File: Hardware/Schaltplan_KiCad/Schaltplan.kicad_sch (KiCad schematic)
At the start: 59 parts, among them J1 3-106505-2, J2 USB_B_Micro, J3 Conn_01x04_Pin, J4 Conn_01x02_Pin, SW1 SW_Omron_B3FS, SW2 SW_Omron_B3FS, SW3 SW_Omron_B3FS, U1 MCP2562-E-SN, U2 FT231XS, U3 ESP32-DEVKITC-32U, U4 AZ1117-5.0, U5 PCA9306DCTR

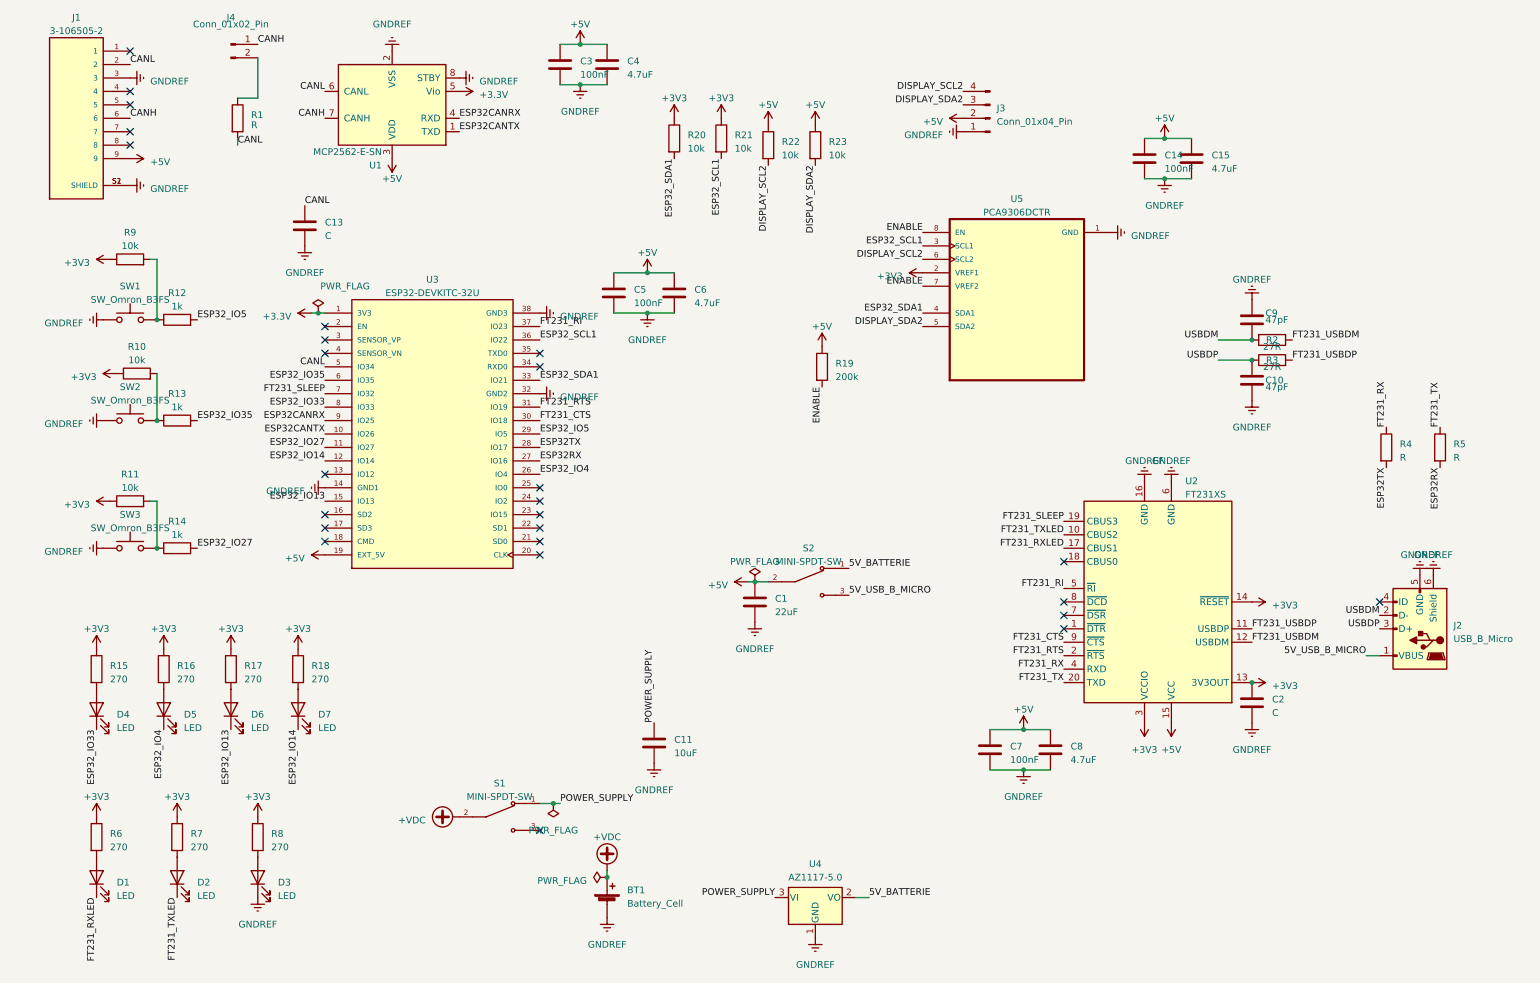
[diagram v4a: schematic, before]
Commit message: changed switch and ldo
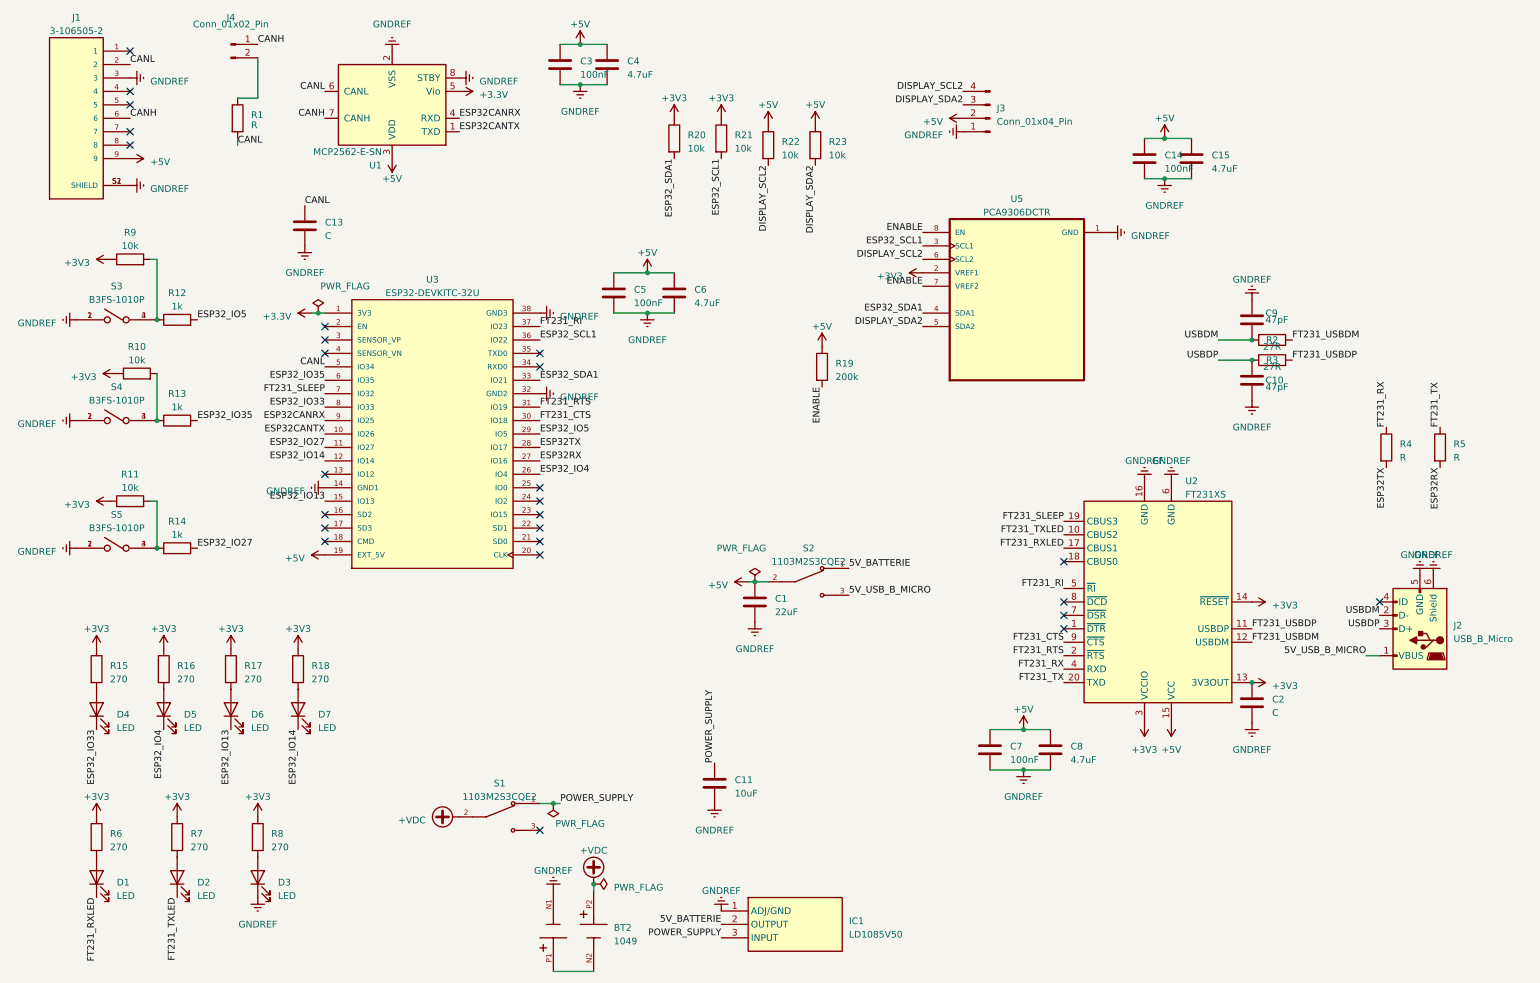
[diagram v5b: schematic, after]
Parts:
- removed BT1: Battery_Cell, symbol Device:Battery_Cell
- removed SW1, SW2, SW3: SW_Omron_B3FS, Button:SW_B3FS-1010P, symbol Switch:SW_Omron_B3FS
- removed U4: AZ1117-5.0, LDO:SOT150P410X160-3N, symbol Regulator_Linear:AZ1117-5.0
- added BT2: 1049, battery_holder:BAT_1049, symbol 1049:1049
- added IC1: LD1085V50, LDO:TO255P460X1020X2008-3P, symbol LD1085V50:LD1085V50
- added S3, S4, S5: B3FS-1010P, SW_B3FS-1010P, symbol B3FS-1010P:B3FS-1010P
- S1, S2: value MINI-SPDT-SW -> 1103M2S3CQE2; footprint switches:SW_MINI-SPDT-SW -> switches:SW_1103M2S3CQE2
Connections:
- net +VDC: now also BT2.P2
- net 5V_BATTERIE: now also IC1.2 (OUTPUT)
- net GNDREF: now also BT2.N1, IC1.1 (ADJ/GND), S3.1, S3.2, S4.1, S4.2, S5.1, S5.2
- net POWER_SUPPLY: now also IC1.3 (INPUT)
- net at R11.2, R14.1: now also S5.3, S5.4
- net at R10.2, R13.1: now also S4.3, S4.4
- net at R12.1, R9.2: now also S3.3, S3.4
- new net: BT2.N2, BT2.P1
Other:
- moved on the sheet: C11

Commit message: placed components on pcb
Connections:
- net +3.3V is gone; now on net +3V3: U1.5 (Vio), U3.1 (3V3)
- net +3V3: no longer C2.1, R6.1, R7.1, R8.1, U2.13 (3V3OUT), U2.14 (~{RESET}), U2.3 (VCCIO)
- net +5V: now also R8.1
- new net FT231_3V3_OUT: C2.1, R6.1, R7.1, U2.13 (3V3OUT), U2.14 (~{RESET}), U2.3 (VCCIO)

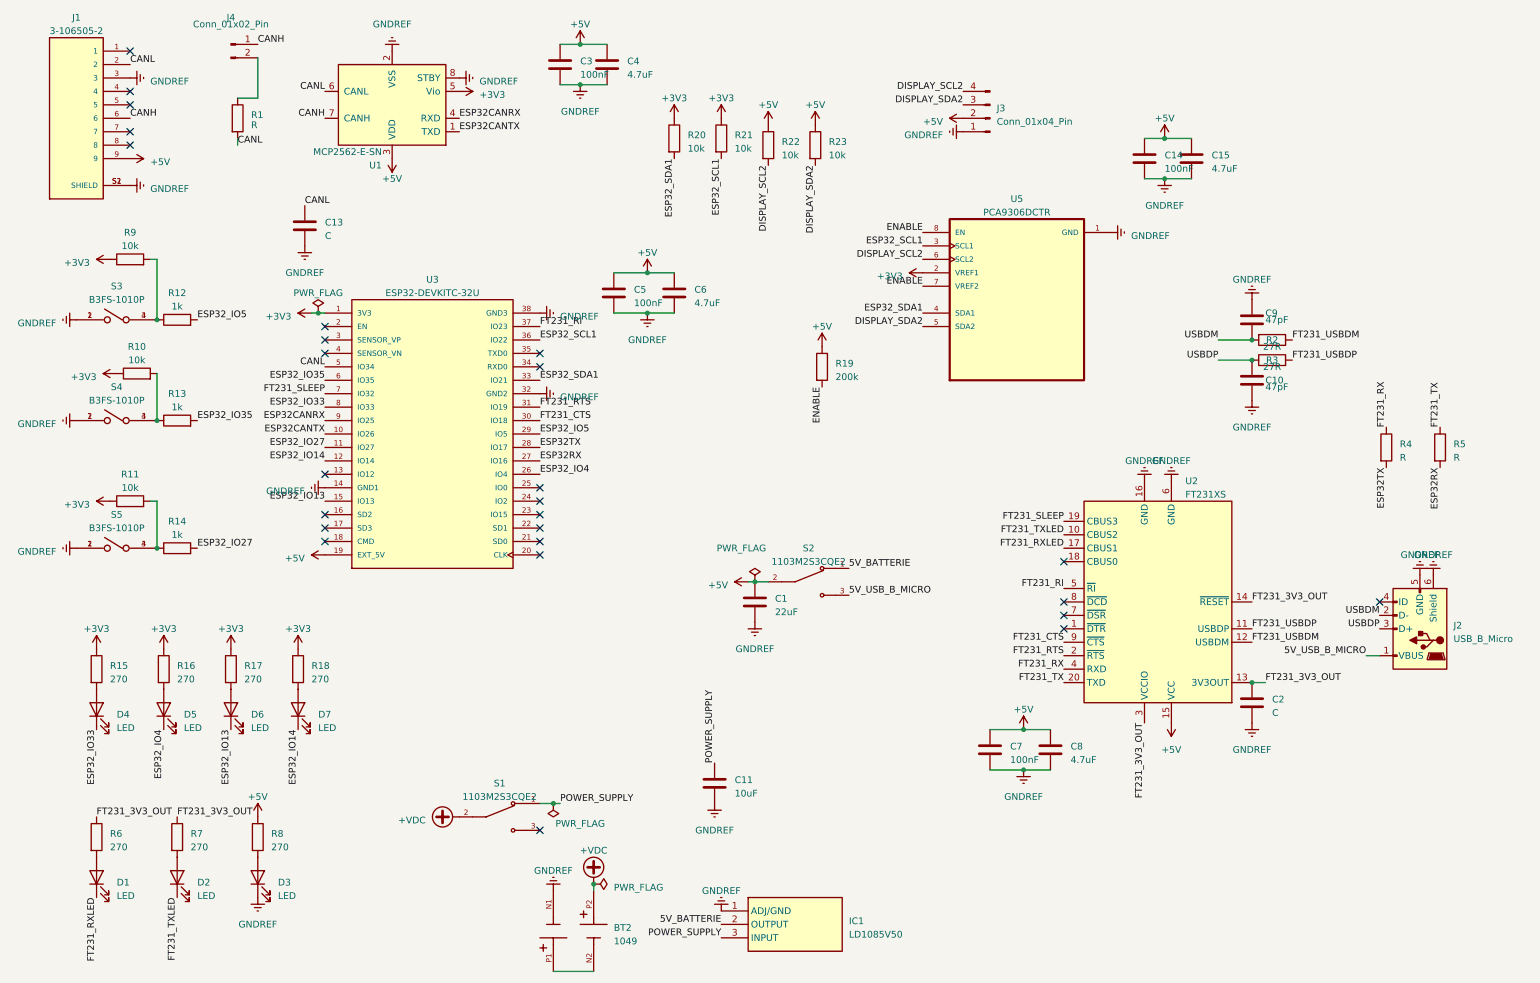
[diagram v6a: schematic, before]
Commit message: remove battery and redesign
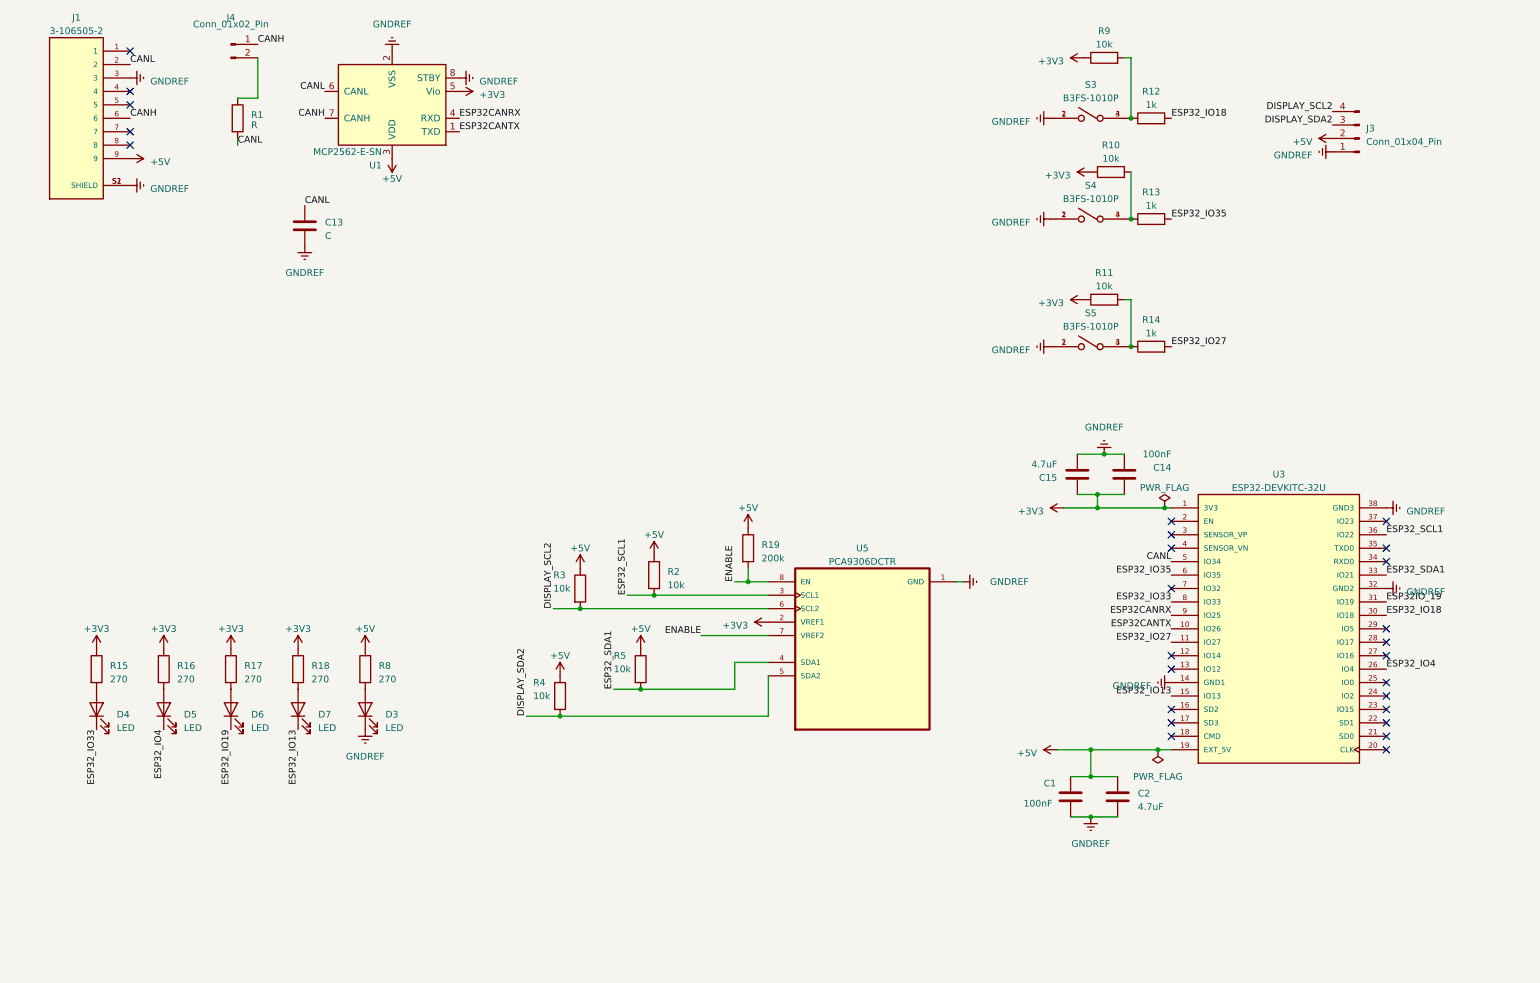
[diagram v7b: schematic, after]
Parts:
- removed BT2: 1049, battery_holder:BAT_1049, symbol 1049:1049
- removed C10, C9: 47pF, Capacitor_SMD:C_1812_4532Metric_Pad1.57x3.40mm_HandSolder, symbol Device:C
- removed C11: 10uF, Capacitor_SMD:C_1812_4532Metric_Pad1.57x3.40mm_HandSolder, symbol Device:C
- removed C3, C5, C7: 100nF, Capacitor_SMD:C_1812_4532Metric_Pad1.57x3.40mm_HandSolder, symbol Device:C
- removed C4, C6, C8: 4.7uF, Capacitor_SMD:C_1812_4532Metric_Pad1.57x3.40mm_HandSolder, symbol Device:C
- removed D1, D2: LED, LED:LED_OF-SMD3528WC, symbol Device:LED
- removed IC1: LD1085V50, LDO:TO255P460X1020X2008-3P, symbol LD1085V50:LD1085V50
- removed J2: USB_B_Micro, Connector_USB:USB_Micro-B_Amphenol_10103594-0001LF_Horizontal, symbol Connector:USB_B_Micro
- removed R20, R21, R22, R23: 10k, Resistor_SMD:R_2010_5025Metric_Pad1.40x2.65mm_HandSolder, symbol Device:R
- removed R6, R7: 270, Resistor_SMD:R_2010_5025Metric_Pad1.40x2.65mm_HandSolder, symbol Device:R
- removed S1, S2: 1103M2S3CQE2, switches:SW_1103M2S3CQE2, symbol MINI-SPDT-SW:MINI-SPDT-SW
- removed U2: FT231XS, USB2UART:SOP63P600X175-20N, symbol Interface_USB:FT231XS
- C1: value 22uF -> 100nF
- C2: value C -> 4.7uF
- R2, R3: value 27R -> 10k
- R4, R5: value R -> 10k
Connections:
- net FT231_3V3_OUT is gone; now on net +5V: C2.1
- net FT231_RX is gone; now on net +5V: R4.1
- net FT231_TX is gone; now on net +5V: R5.1
- net FT231_USBDM is gone; now on net +5V: R2.1
- net FT231_USBDP is gone; now on net DISPLAY_SCL2: R3.2
- net USBDM is gone; now on net ESP32_SCL1: R2.2
- net USBDP is gone; now on net +5V: R3.1
- net +3V3: now also C14.1, C15.1
- net +5V: no longer C14.1, C15.1
- net DISPLAY_SDA2: now also R4.2
- net ESP32_IO13: now also D7.1 (K); no longer D6.1 (K)
- net ESP32_SDA1: now also R5.2
- net ESP32RX: no longer names the net of U3.27 (IO16)
- net ESP32RX: no longer R5.2
- net ESP32TX: no longer names the net of U3.28 (IO17)
- net ESP32TX: no longer R4.2
- net ESP32_IO14: no longer names the net of U3.12 (IO14)
- net ESP32_IO14: no longer D7.1 (K)
- net ESP32_IO5: no longer names the net of U3.29 (IO5)
- net ESP32_IO5: no longer R12.2
- net FT231_CTS renamed ESP32_IO18
- net ESP32_IO18: now also R12.2
- net FT231_RI: no longer names the net of U3.37 (IO23)
- net FT231_RTS renamed ESP32IO_19
- net FT231_SLEEP: no longer names the net of U3.7 (IO32)
- new net ESP32_IO19: D6.1 (K)
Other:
- moved on the sheet: C14, C15, D3, J3, R10, R11, R12, R13, R14, R19, R8, R9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

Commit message: finishes PCB Design
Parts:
- removed C13: C, Capacitor_SMD:C_1812_4532Metric_Pad1.57x3.40mm_HandSolder, symbol Device:C
- C1, C14, C15, C2: footprint Capacitor_SMD:C_1812_4532Metric_Pad1.57x3.40mm_HandSolder -> Capacitor_SMD:C_0603_1608Metric_Pad1.08x0.95mm_HandSolder
- R1: value R -> 120R; footprint Resistor_SMD:R_2010_5025Metric_Pad1.40x2.65mm_HandSolder -> Resistor_SMD:R_0603_1608Metric_Pad0.98x0.95mm_HandSolder
- R10, R11, R12, R13, R14, R15, R16, R17, R18, R19, R2, R3, R4, R5, R8, R9: footprint Resistor_SMD:R_2010_5025Metric_Pad1.40x2.65mm_HandSolder -> Resistor_SMD:R_0603_1608Metric_Pad0.98x0.95mm_HandSolder
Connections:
- net ESP32IO_19 is gone; now on net ESP32_IO19: U3.31 (IO19)
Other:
- moved on the sheet: C1, C14, C15, C2, D3, D4, D5, D6, D7, J1, J4, R1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
